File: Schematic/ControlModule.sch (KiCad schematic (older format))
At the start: 9 parts, among them SW1 Backlight control, U10 LCDSerial2004, U6 ArduinoNano, U7 ESP-01, U8 AMS1117-33

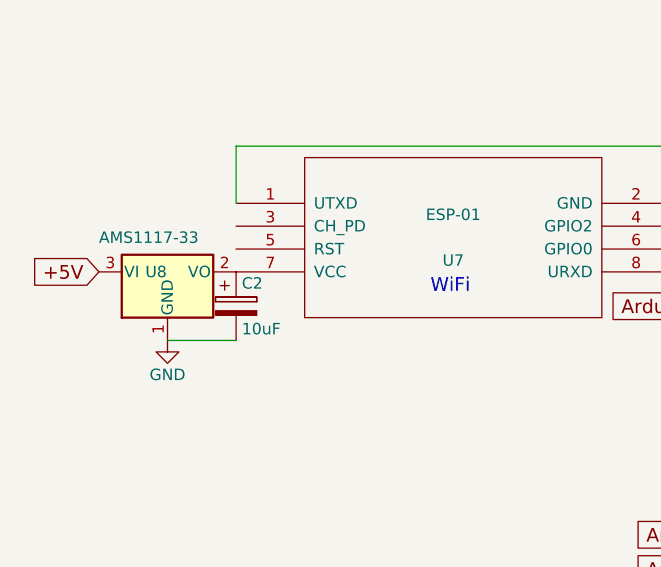
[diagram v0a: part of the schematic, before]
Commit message: added BOM, started Fritzing prototype diagram, minor layout changes in KiCad
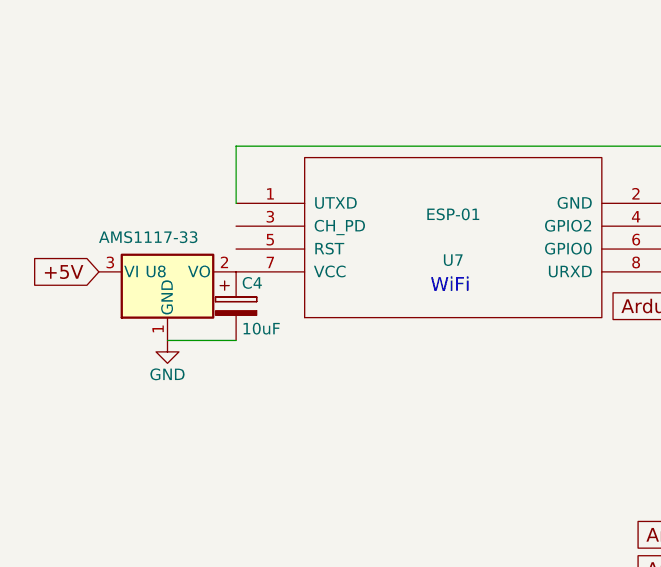
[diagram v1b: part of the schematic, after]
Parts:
- renumbered C2 to C4
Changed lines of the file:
@@
 	7850 1400 7100 1400
 $Comp
-L GND #PWR15
+L GND #PWR015
 U 1 1 5AC8E582
 P 8200 1200
-F 0 "#PWR15" H 8200 950 50  0001 C CNN
+F 0 "#PWR015" H 8200 950 50  0001 C CNN
 F 1 "GND" H 8200 1050 50  0000 C CNN
 F 2 "" H 8200 1200 50  0001 C CNN
@@
 	4750 1850 5000 1850
 $Comp
-L GND #PWR16
+L GND #PWR016
 U 1 1 5AC8E9E4
 P 4850 1850
-F 0 "#PWR16" H 4850 1600 50  0001 C CNN
+F 0 "#PWR016" H 4850 1600 50  0001 C CNN
 F 1 "GND" H 4850 1700 50  0000 C CNN
 F 2 "" H 4850 1850 50  0001 C CNN
@@
 +5V
 $Comp
-L GND #PWR17
+L GND #PWR017
 U 1 1 5AC8EB1F
 P 2550 2450
-F 0 "#PWR17" H 2550 2200 50  0001 C CNN
+F 0 "#PWR017" H 2550 2200 50  0001 C CNN
 F 1 "GND" H 2550 2300 50  0000 C CNN
 F 2 "" H 2550 2450 50  0001 C CNN
@@
 	5750 1600 6100 1600
 $Comp
-L CP C2
+L CP C4
 U 1 1 5AC8FDDC
 P 2850 2300
-F 0 "C2" H 2875 2400 50  0000 L CNN
+F 0 "C4" H 2875 2400 50  0000 L CNN
 F 1 "10uF" H 2875 2200 50  0000 L CNN
 F 2 "" H 2888 2150 50  0001 C CNN
@@
 +5V
 $Comp
-L GND #PWR18
+L GND #PWR018
 U 1 1 5AC9C12A
 P 5750 3500
-F 0 "#PWR18" H 5750 3250 50  0001 C CNN
+F 0 "#PWR018" H 5750 3250 50  0001 C CNN
 F 1 "GND" H 5750 3350 50  0000 C CNN
 F 2 "" H 5750 3500 50  0001 C CNN
@@
 $EndComp
 $Comp
-L GND #PWR19
+L GND #PWR019
 U 1 1 5AC9C2C9
 P 7550 3600
-F 0 "#PWR19" H 7550 3350 50  0001 C CNN
+F 0 "#PWR019" H 7550 3350 50  0001 C CNN
 F 1 "GND" H 7550 3450 50  0000 C CNN
 F 2 "" H 7550 3600 50  0001 C CNN

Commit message: Minor corrections. Combined 3 sheets into a single schematic
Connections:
- wire segments 32 -> 33
- no-connect marks 0 -> 8
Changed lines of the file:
@@
 Sheet 4 4
 Title "XL4016X2"
-Date "2018-01-11"
-Rev ""
+Date "2018-04-11"
+Rev "V3 minor corrections"
 Comp "farmerkeith"
 Comment1 ""
@@
 Text GLabel 7550 3250 2    60   Input ~ 0
 Arduino_pin_A6
+Wire Wire Line
+	2850 1950 2850 2150
+Connection ~ 2850 2050
+Connection ~ 2850 2150
+NoConn ~ 4750 1950
+NoConn ~ 4750 2050
+NoConn ~ 6100 2400
+NoConn ~ 6100 2500
+NoConn ~ 7100 2500
+NoConn ~ 7100 2400
+NoConn ~ 7100 2300
+NoConn ~ 7100 2200
 $EndSCHEMATC
